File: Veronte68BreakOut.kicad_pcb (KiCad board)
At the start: 2 copper layers, 11 parts, among them J1 DC37_Receptacle_MountingHoles, J10 Barrel_Jack_Switch, J11 Barrel_Jack_Switch, J2 DC37_Receptacle_MountingHoles, J3 DE9_Receptacle_MountingHoles, J4 Conn_01x19, J5 Conn_01x11, J6 Conn_01x19, J7 Conn_01x11, J8 Conn_01x05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

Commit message: pcbを作成
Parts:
- moved J10 95.5 mm to (87.6, 198.1), turned to -90 degrees
- moved J9 80.3 mm to (76.2, 221.0)
- moved J5 41.8 mm to (73.7, 38.1)
- moved J8 41.6 mm to (127.0, 221.0)
- moved J11 41.3 mm to (87.6, 170.2), turned to -90 degrees
- moved J7 40.8 mm to (73.7, 124.5)
- moved J3 32.2 mm to (185.1, 220.5)
- moved J4 27.9 mm to (127.0, 38.1)
- moved J2 27.9 mm to (184.0, 123.7)
- moved J1 27.7 mm to (184.0, 37.3)
- moved J6 26.7 mm to (127.0, 124.5)
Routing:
- net Net-(J8-Pin_5): track 0.00 -> 261.8 mm
- net Net-(J9-Pin_2): track 0.00 -> 195.6 mm
- net Net-(J7-Pin_2): track 0.00 -> 114.1 mm
- net Net-(J7-Pin_1): track 0.00 -> 113.9 mm
- net Net-(J7-Pin_6): track 0.00 -> 113.9 mm
- net Net-(J7-Pin_5): track 0.00 -> 113.8 mm
- net Net-(J7-Pin_3): track 0.00 -> 113.8 mm
- net Net-(J7-Pin_4): track 0.00 -> 113.7 mm
- net Net-(J6-Pin_17): track 0.00 -> 107.5 mm
- net Net-(J6-Pin_18): track 0.00 -> 98.8 mm
- net Net-(J6-Pin_19): track 0.00 -> 58.4 mm
- net Net-(J6-Pin_1): track 0.00 -> 57.3 mm
- net Net-(J6-Pin_7): track 0.00 -> 57.2 mm
- net Net-(J6-Pin_2): track 0.00 -> 57.2 mm
- net Net-(J6-Pin_6): track 0.00 -> 57.1 mm
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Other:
- board outline added: 137.2 x 228.6 mm
- board text added: "1: I/O1 I/O 2: I/O2 I/O 3: I/O3 I/O 4: I/O4 I/O 5: I/O5 I/O 6: I/O6 I/O 7: I/O7 I/O 8: I/O8 I/O 9: GND GROUND 10: I/O9 I/O 11: I/O10 I/O 12: I/O11 I/O 13: I/O12 I/O 14: I/O13 I/O 15: I/O14 I/O 16: I/O15 I/O 17: I/O16 I/O 18: GND GROUND 19: RS 232 TX Output"
- board text added: "20: RS 232 RX Input 21: GND GROUND 22: Analog 4 Input Analog 23: Analog 5 Input Analog 24: GND GROUND 25: CanA P I/O 26: CanA N I/O 27: GND GROUND 28: CANB_P I/O 29: CANB_N I/O 30: GND GROUND"
- board text added: "31: I2C_CLK Output 32: I2C_DATA I/O 33: GND GROUND 34: 3.3V POWER 35: GND GROUND 36: 5V POWER 37: GND GROUND 38: ANALOG_1 Input 39: ANALOG_2 Input 40: ANALOG_3 Input 41: GND GROUND 42: FTS1_OUT Output 43: FTS2_OUT Output 44: GND GROUND 45: V_ARB_TX Output 46: V_ARB_RX Input 47: GND GROUND 48: V_ARB_VCC POWER 49: FTS3_OUT_MPU Output"
- board text added: "50: OUT_RS485_P Output 51: OUT_RS485_N Output 52: IN_RS845_N Input 53: IN_RS845_P Input 54: RS-485_GND GND 55: EQEP_A I/O 56: EQEP_B I/O 57: EQEP_S I/O 58: EQEP_I I/O 59: GND GROUND 60: V_USB_DP I/O"
- board text added: "61: V_USB_DN I/O 62: V_USB_ID I/O 63: FTS_OUT_MPU Output 64: FTS2_OUT_MPU Output 65: GND GROUND"
- board text added: "66: GND GROUND 67: VCC POWER 68: VCC POWER"
- board text added: "DC1 -: 65,66 GND +: 67,68 VCC"
- board text added: "DC2 -: 47 GND +: 48 V_ARB_VCC"

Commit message: rooting finish
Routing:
- net Net-(J7-Pin_11): track 0.00 -> 115.4 mm
- net Net-(J5-Pin_11): track 0.00 -> 114.4 mm
- net Net-(J7-Pin_10): track 0.00 -> 114.3 mm
- net Net-(J5-Pin_10): track 0.00 -> 114.3 mm
- net Net-(J7-Pin_9): track 0.00 -> 114.2 mm
- net Net-(J5-Pin_9): track 0.00 -> 114.2 mm
- net Net-(J7-Pin_8): track 0.00 -> 114.1 mm
- net Net-(J5-Pin_8): track 0.00 -> 114.1 mm
- net Net-(J7-Pin_7): track 0.00 -> 114.0 mm
- net Net-(J5-Pin_7): track 0.00 -> 114.0 mm
- net Net-(J5-Pin_1): track 0.00 -> 113.9 mm
- net Net-(J5-Pin_6): track 0.00 -> 113.9 mm
- net Net-(J5-Pin_2): track 0.00 -> 113.8 mm
- net Net-(J5-Pin_5): track 0.00 -> 113.8 mm
- net Net-(J5-Pin_3): track 0.00 -> 113.8 mm
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
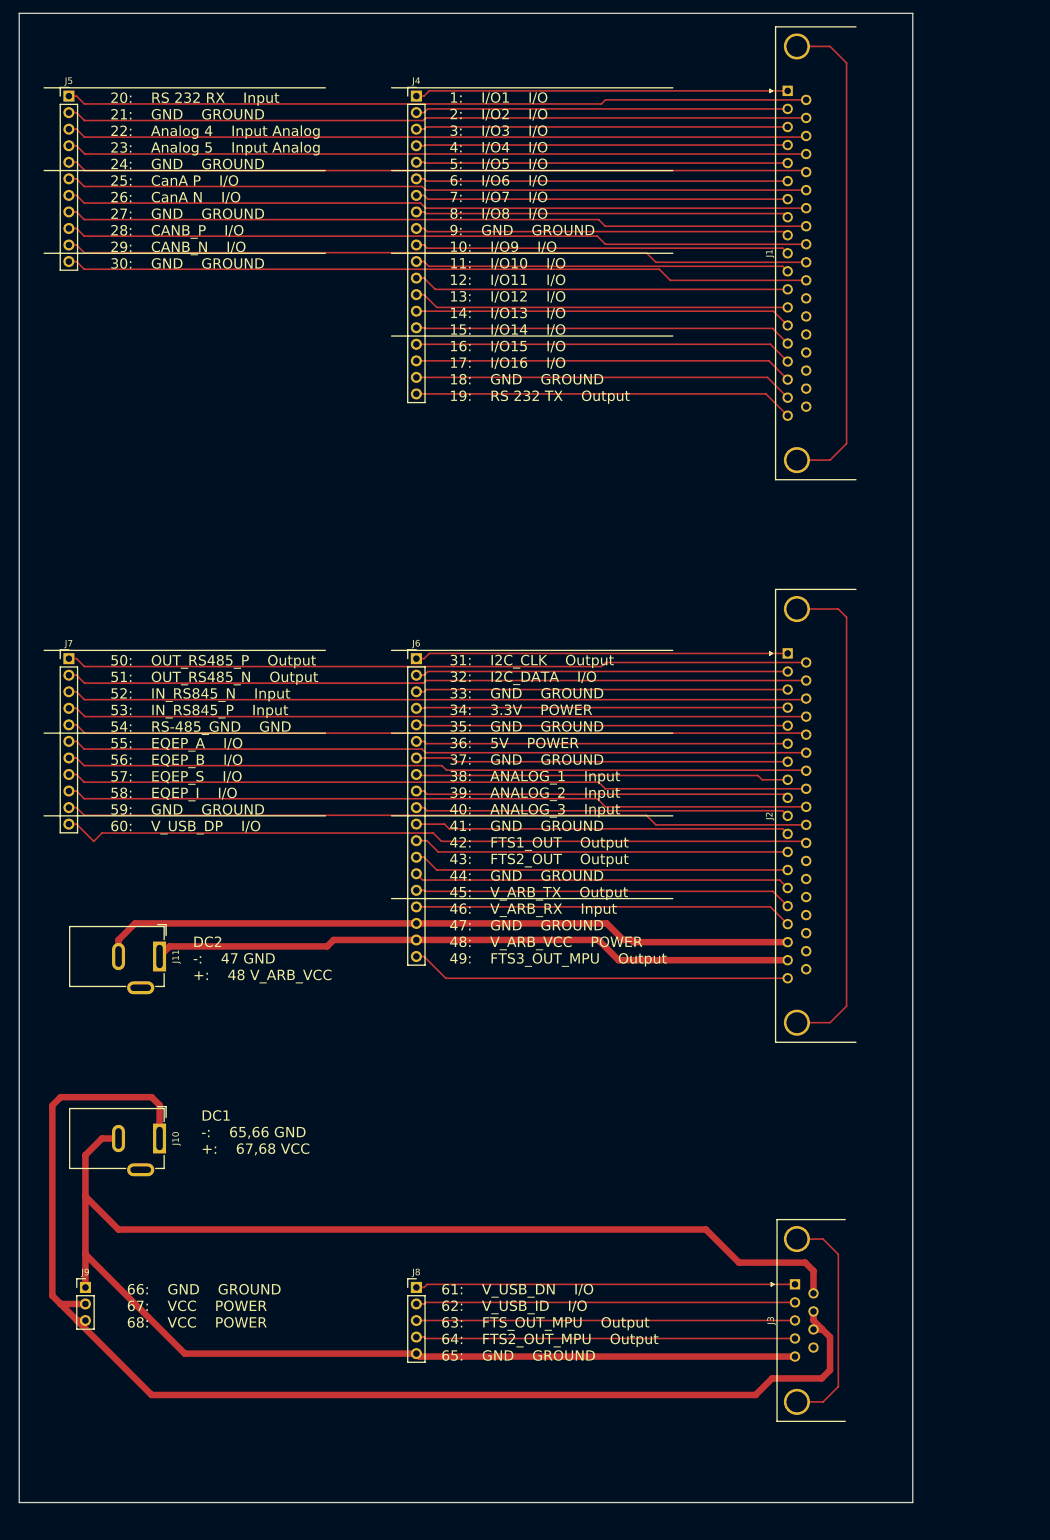
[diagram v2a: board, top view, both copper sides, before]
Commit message: add silkscreen
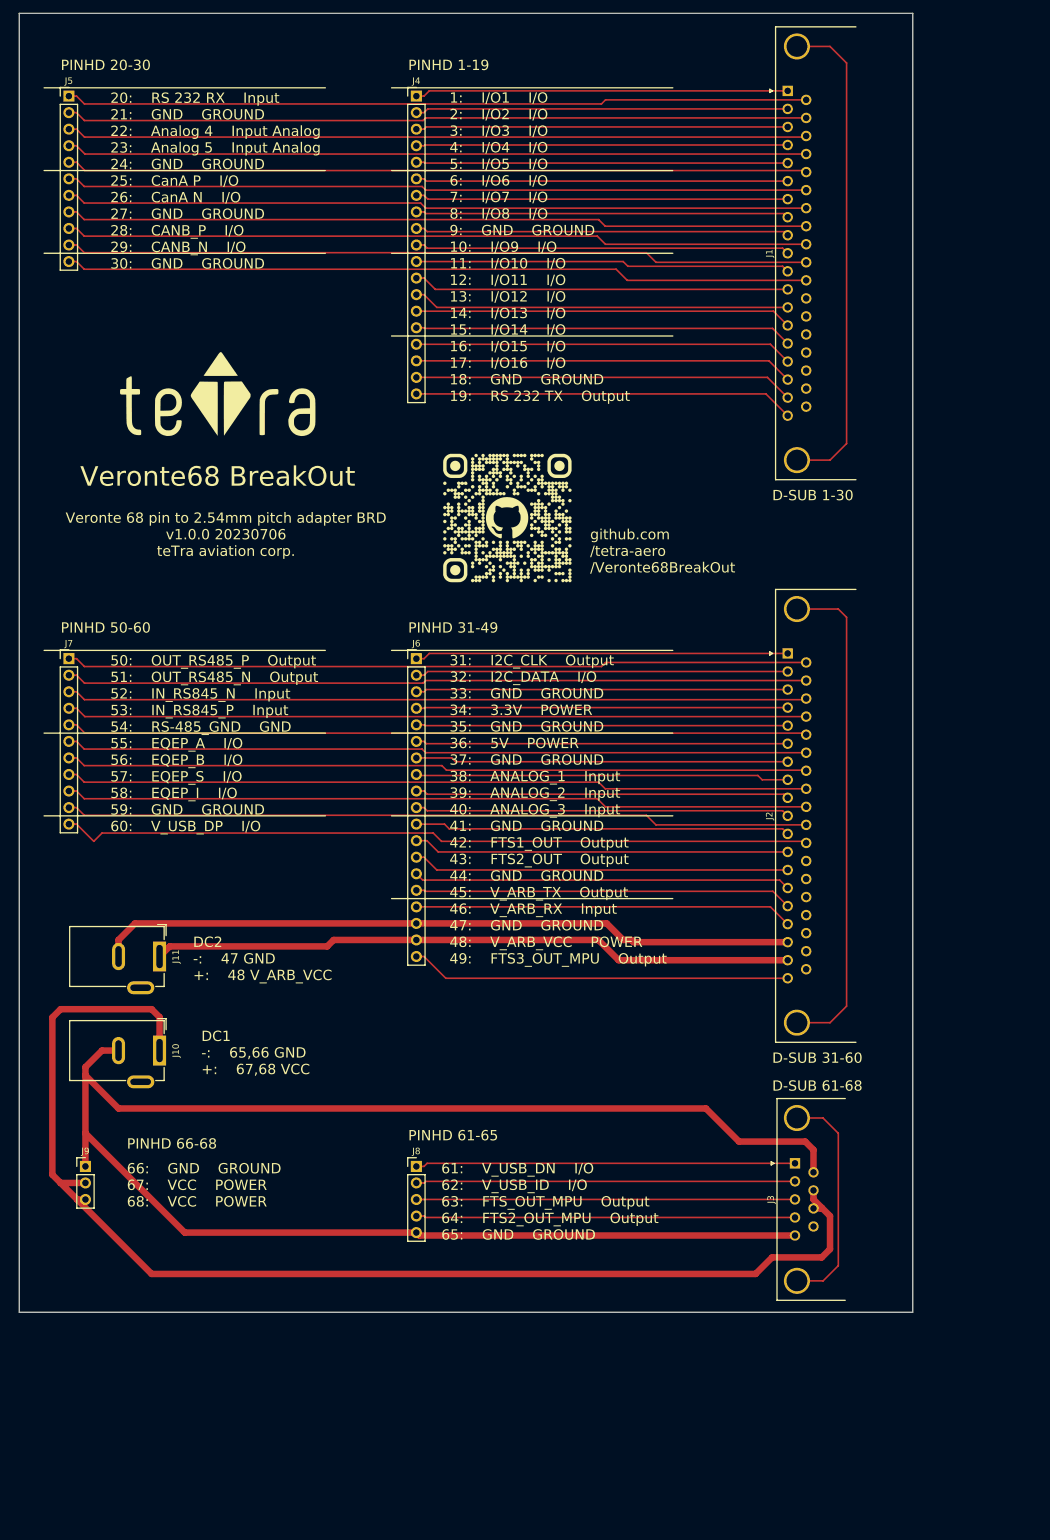
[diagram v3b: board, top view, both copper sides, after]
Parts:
- added G***: LOGO, LOGO, F.Cu at (96.5, 83.8)
- added G***: LOGO, LOGO, F.Cu at (141.0, 102.9)
- moved J3 18.6 mm to (185.1, 201.9)
- moved J8 18.6 mm to (127.0, 202.4)
- moved J9 18.6 mm to (76.2, 202.4)
- moved J10 13.5 mm to (87.6, 184.6)
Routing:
- net Net-(J8-Pin_5): track 261.8 -> 256.7 mm
- net Net-(J9-Pin_2): track 195.6 -> 190.5 mm
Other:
- board size 137.2 x 228.6 mm -> 137.2 x 199.4 mm
- board text added: "D-SUB 1-30"
- board text added: "D-SUB 31-60"
- board text added: "D-SUB 61-68"
- board text added: "PINHD 1-19"
- board text added: "PINHD 20-30"
- board text added: "PINHD 31-49"
- board text added: "PINHD 50-60"
- board text added: "PINHD 61-65"
- board text added: "PINHD 66-68"
- board text added: "Veronte 68 pin to 2.54mm pitch adapter BRD v1.0.0 20230706 teTra aviation corp."
- board text added: "Veronte68 BreakOut"
- board text added: "github.com /tetra-aero /Veronte68BreakOut"

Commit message: add v1.3
- change 60/61/62 pin
- change number of pin header
- add GND and solid GND pattern
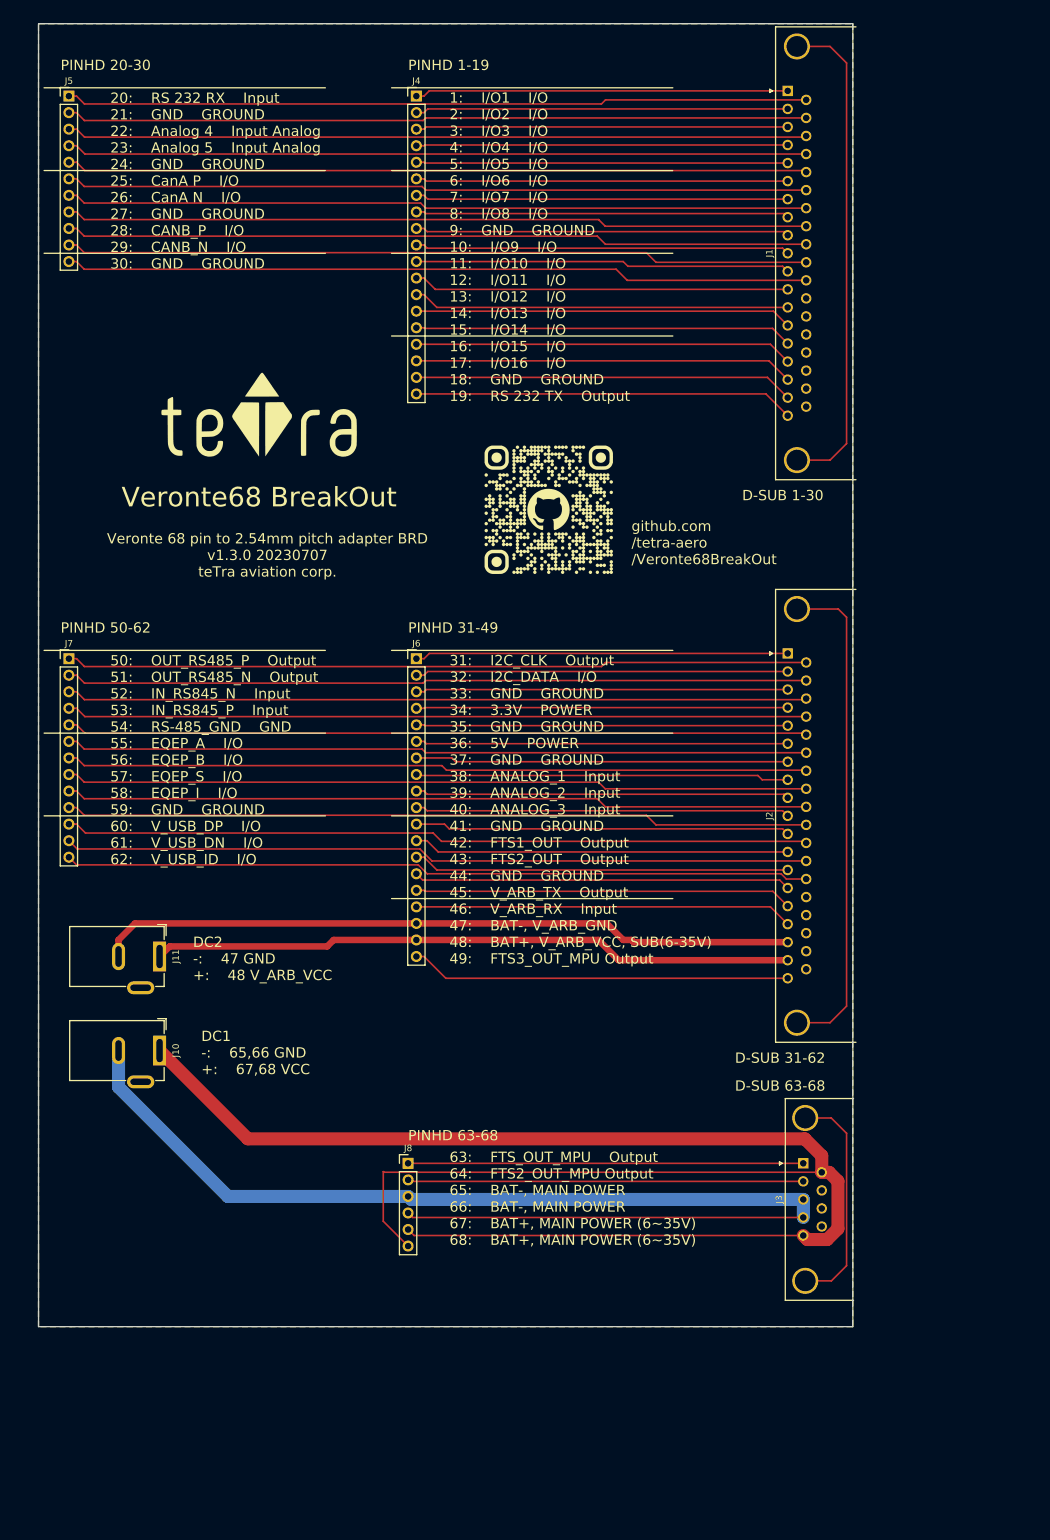
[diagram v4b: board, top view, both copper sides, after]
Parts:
- removed J9: Conn_01x03, Connector_PinHeader_2.54mm:PinHeader_1x03_P2.54mm_Vertical
- J7: value Conn_01x11 -> Conn_01x13; footprint Connector_PinHeader_2.54mm:PinHeader_1x11_P2.54mm_Vertical -> Connector_PinHeader_2.54mm:PinHeader_1x13_P2.54mm_Vertical
- J8: value Conn_01x05 -> Conn_01x06; footprint Connector_PinHeader_2.54mm:PinHeader_1x05_P2.54mm_Vertical -> Connector_PinHeader_2.54mm:PinHeader_1x06_P2.54mm_Vertical
- moved G*** 7.10 mm to (102.9, 87.0)
- moved G*** 6.48 mm to (147.3, 101.6)
- moved J8 1.35 mm to (125.7, 201.9)
- moved J3 1.27 mm to (186.4, 201.9)
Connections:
- J1 pad 18: Net-(J4-Pin_18) -> GND
- J1 pad 21: Net-(J5-Pin_2) -> GND
- J1 pad 24: Net-(J5-Pin_5) -> GND
- J1 pad 27: Net-(J5-Pin_8) -> GND
- J1 pad 30: Net-(J5-Pin_11) -> GND
- J1 pad 9: Net-(J4-Pin_9) -> GND
- J10 pad 1: Net-(J9-Pin_2) -> Net-(J8-Pin_5)
- J10 pad 2: Net-(J8-Pin_5) -> Net-(J8-Pin_3)
- J2 pad 11: Net-(J6-Pin_11) -> GND
- J2 pad 14: Net-(J6-Pin_14) -> GND
- J2 pad 22: Net-(J7-Pin_3) -> GND
- J2 pad 24: Net-(J7-Pin_5) -> GND
- J2 pad 29: Net-(J7-Pin_10) -> GND
- J2 pad 31: unconnected-(J2-Pad31) -> Net-(J7-Pin_12)
- J2 pad 32: unconnected-(J2-Pad32) -> Net-(J7-Pin_13)
- J2 pad 5: Net-(J6-Pin_5) -> GND
- J2 pad 7: Net-(J6-Pin_7) -> GND
- J3 pad 4: Net-(J8-Pin_4) -> Net-(J8-Pin_3)
- J3 pad 7: Net-(J9-Pin_2) -> unconnected-(J3-Pad7)
- J3 pad 8: Net-(J9-Pin_2) -> unconnected-(J3-Pad8)
- J4 pad 18: Net-(J4-Pin_18) -> GND
- J4 pad 9: Net-(J4-Pin_9) -> GND
- J5 pad 11: Net-(J5-Pin_11) -> GND
- J5 pad 2: Net-(J5-Pin_2) -> GND
- J5 pad 5: Net-(J5-Pin_5) -> GND
- J5 pad 8: Net-(J5-Pin_8) -> GND
- J6 pad 11: Net-(J6-Pin_11) -> GND
- J6 pad 14: Net-(J6-Pin_14) -> GND
- J6 pad 5: Net-(J6-Pin_5) -> GND
- J6 pad 7: Net-(J6-Pin_7) -> GND
- J7 pad 10: Net-(J7-Pin_10) -> GND
- J7 pad 3: Net-(J7-Pin_3) -> GND
- J7 pad 5: Net-(J7-Pin_5) -> GND
- J8 pad 4: Net-(J8-Pin_4) -> Net-(J8-Pin_3)
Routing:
- net GND: track 0.00 -> 1143.5 mm
- net Net-(J9-Pin_2): track 190.5 -> 0.00 mm
- net Net-(J8-Pin_3): track 58.1 -> 181.6 mm
- net Net-(J7-Pin_13): track 0.00 -> 114.6 mm
- net Net-(J7-Pin_12): track 0.00 -> 114.5 mm
- net Net-(J5-Pin_11): track 114.4 -> 0.00 mm
- net Net-(J7-Pin_10): track 114.3 -> 0.00 mm
- net Net-(J5-Pin_8): track 114.1 -> 0.00 mm
- net Net-(J5-Pin_2): track 113.8 -> 0.00 mm
- net Net-(J7-Pin_5): track 113.8 -> 0.00 mm
- net Net-(J5-Pin_5): track 113.8 -> 0.00 mm
- net Net-(J7-Pin_3): track 113.8 -> 0.00 mm
- net Net-(J4-Pin_18): track 58.3 -> 0.00 mm
- net Net-(J8-Pin_4): track 58.2 -> 0.00 mm
- net Net-(J6-Pin_14): track 57.9 -> 0.00 mm
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- added copper zone on B.Cu, net GND
- added copper zone on F.Cu, net GND
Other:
- board size 137.2 x 199.4 mm -> 125 x 200 mm
- board text added: "31: I2C_CLK Output 32: I2C_DATA I/O 33: GND GROUND 34: 3.3V POWER 35: GND GROUND 36: 5V POWER 37: GND GROUND 38: ANALOG_1 Input 39: ANALOG_2 Input 40: ANALOG_3 Input 41: GND GROUND 42: FTS1_OUT Output 43: FTS2_OUT Output 44: GND GROUND 45: V_ARB_TX Output 46: V_ARB_RX Input 47: BAT-, V_ARB_GND 48: BAT+, V_ARB_VCC, SUB(6-35V) 49: FTS3_OUT_MPU Output"
- board text added: "50: OUT_RS485_P Output 51: OUT_RS485_N Output 52: IN_RS845_N Input 53: IN_RS845_P Input 54: RS-485_GND GND 55: EQEP_A I/O 56: EQEP_B I/O 57: EQEP_S I/O 58: EQEP_I I/O 59: GND GROUND 60: V_USB_DP I/O 61: V_USB_DN I/O 62: V_USB_ID I/O"
- board text added: "63: FTS_OUT_MPU Output 64: FTS2_OUT_MPU Output 65: BAT-, MAIN POWER 66: BAT-, MAIN POWER 67: BAT+, MAIN POWER (6~35V) 68: BAT+, MAIN POWER (6~35V)"
- board text added: "D-SUB 31-62"
- board text added: "D-SUB 63-68"
- board text added: "PINHD 50-62"
- board text added: "PINHD 63-68"
- board text added: "Veronte 68 pin to 2.54mm pitch adapter BRD v1.3.0 20230707 teTra aviation corp."
- board text removed: "31: I2C_CLK Output 32: I2C_DATA I/O 33: GND GROUND 34: 3.3V POWER 35: GND GROUND 36: 5V POWER 37: GND GROUND 38: ANALOG_1 Input 39: ANALOG_2 Input 40: ANALOG_3 Input 41: GND GROUND 42: FTS1_OUT Output 43: FTS2_OUT Output 44: GND GROUND 45: V_ARB_TX Output 46: V_ARB_RX Input 47: GND GROUND 48: V_ARB_VCC POWER 49: FTS3_OUT_MPU Output"
- board text removed: "50: OUT_RS485_P Output 51: OUT_RS485_N Output 52: IN_RS845_N Input 53: IN_RS845_P Input 54: RS-485_GND GND 55: EQEP_A I/O 56: EQEP_B I/O 57: EQEP_S I/O 58: EQEP_I I/O 59: GND GROUND 60: V_USB_DP I/O"
- board text removed: "61: V_USB_DN I/O 62: V_USB_ID I/O 63: FTS_OUT_MPU Output 64: FTS2_OUT_MPU Output 65: GND GROUND"
- board text removed: "66: GND GROUND 67: VCC POWER 68: VCC POWER"
- board text removed: "D-SUB 31-60"
- board text removed: "D-SUB 61-68"
- board text removed: "PINHD 50-60"
- board text removed: "PINHD 61-65"
- board text removed: "PINHD 66-68"
- board text removed: "Veronte 68 pin to 2.54mm pitch adapter BRD v1.0.0 20230706 teTra aviation corp."
